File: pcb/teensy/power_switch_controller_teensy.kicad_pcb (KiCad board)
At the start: 2 copper layers, 77.5 x 40.6 mm, 23 parts, among them P1 PWR_JACK_2.5x5.5_SMD_RA, P2 HEADER_01X03_SMD_RA, P3 HEADER_01X03_SMD_RA, P4 HEADER_01X03_SMD_RA, P5 BNC_DOUBLE_RA, P6 HEADER_01X02_SMD_RA, P7 HEADER_01X02_SMD_RA, SW1 KT_SWITCH

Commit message: More progress towards v1.0.
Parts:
- removed C3, C4, C5: 10uF, power_switch_controller_teensy:SM1210
- removed D1, D2: diode_schottky_15V_1A, power_switch_controller_teensy:DO-214BA
- removed D3, D4: diode_schottky_45V_10A, power_switch_controller_teensy:CFP15
- removed MNT_HOLE1, MNT_HOLE2, MNT_HOLE3: MNT_HOLE, power_switch_controller_teensy:MNT_HOLE
- removed P2, P3, P4: HEADER_01X03_SMD_RA, power_switch_controller_teensy:Header_3_Pin_SMD_RA
- removed P5: BNC_DOUBLE_RA, power_switch_controller_teensy:BNC_DOUBLE
- removed P6, P7: HEADER_01X02_SMD_RA, power_switch_controller_teensy:Header_2_Pin_SMD_RA
- removed REG1: CONV_DC_DC_5V_1A, power_switch_controller_teensy:DC_DC_CONV_R78C
- removed TEENSY1: TEENSY_3_2, power_switch_controller_teensy:TEENSY_3
- added L1: LED_24V, power_switch_controller_teensy:LED_555-3XXX, F.Cu at (82.5, 99.7)
- added L2: LED_24V, power_switch_controller_teensy:LED_555-3XXX, F.Cu at (114.3, 109.2)
- added L3: LED_24V, power_switch_controller_teensy:LED_555-3XXX, F.Cu at (111.8, 109.2)
- added L4: LED_24V, power_switch_controller_teensy:LED_555-3XXX, F.Cu at (109.2, 109.2)
- added L5: LED_24V, power_switch_controller_teensy:LED_555-3XXX, F.Cu at (106.7, 109.2)
- added L6: LED_24V, power_switch_controller_teensy:LED_555-3XXX, F.Cu at (104.1, 109.2)
- added L7: LED_24V, power_switch_controller_teensy:LED_555-3XXX, F.Cu at (101.6, 109.2)
- added L8: LED_24V, power_switch_controller_teensy:LED_555-3XXX, F.Cu at (99.1, 109.2)
- added L9: LED_24V, power_switch_controller_teensy:LED_555-3XXX, F.Cu at (96.5, 109.2)
- added U1: TLE7230R, power_switch_controller_teensy:PG-DSO-36, B.Cu at (123.2, 99.7)
- C2: value 10uF -> 0.1uF
- MDT1: value MODULAR_DEVICE_TEENSY -> MODULAR_DEVICE_TEENSY_MALE
- P1: value PWR_JACK_2.5x5.5_SMD_RA -> HEADER_02X08_SMD; footprint power_switch_controller_teensy:DCJACK_2PIN_HIGHCURRENT_SMD_RA -> power_switch_controller_teensy:HEADER_02x08_SMD; moved to F.Cu
- SW1: value KT_SWITCH -> SPST_SLIDE_AS; footprint power_switch_controller_teensy:KT_SWITCH -> power_switch_controller_teensy:SPST_SLIDE_AS
- moved C2 60.3 mm to (123.2, 111.1), turned to 0 degrees
- moved P1 26.7 mm to (105.4, 99.7)
- moved SW1 21.6 mm to (86.4, 99.7), turned to 0 degrees
- moved C1 20.7 mm to (83.8, 91.4), turned to 180 degrees
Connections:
- C2 pad 1: +5V -> VEE
- MDT1 pad 10: /D10 -> /CS
- MDT1 pad 11: /D11 -> /MOSI
- MDT1 pad 12: /D12 -> /MISO
- MDT1 pad 13: /D13 -> /SCK
- MDT1 pad 14: /D14 -> (no net)
- MDT1 pad 15: /D15 -> (no net)
- MDT1 pad 16: /D16 -> (no net)
- MDT1 pad 17: /D17 -> (no net)
- MDT1 pad 18: /D18 -> (no net)
- MDT1 pad 19: /D19 -> (no net)
- MDT1 pad 2: /D2 -> /RESET
- MDT1 pad 20: /D20 -> (no net)
- MDT1 pad 21: /D21 -> (no net)
- MDT1 pad 22: /D22 -> (no net)
- MDT1 pad 23: /D23 -> (no net)
- MDT1 pad 24: /D24 -> (no net)
- MDT1 pad 25: /D25 -> (no net)
- MDT1 pad 28: /D28 -> (no net)
- MDT1 pad 29: /D29 -> (no net)
- MDT1 pad 3: /D3 -> /PWM
- MDT1 pad 30: /D30 -> (no net)
- MDT1 pad 3V3: /3V3 -> (no net)
- MDT1 pad 4: /D4 -> (no net)
- MDT1 pad 5: /D5 -> (no net)
- MDT1 pad 6: /D6 -> (no net)
- MDT1 pad 9: /D9 -> (no net)
- MDT1 pad AGND: /AGND -> (no net)
- MDT1 pad AREF: /AREF -> (no net)
- MDT1 pad DAC: /DAC -> (no net)
- P1 pad 1: VAA -> VDD
- P1 pad 2: GND -> /OUT0
- P1 pad 3: (no net) -> VDD
- SW1 pad 1: (no net) -> VDD
- SW1 pad 3: GND -> /LED_PWR
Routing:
- net (no net): track 0.00 -> 570.8 mm, vias 0 -> 4
- net /OUT3: track 0.00 -> 89.8 mm, vias 0 -> 2
- net VAA: track 85.8 -> 0.00 mm, vias 2 -> 0
- net /OUT4: track 0.00 -> 73.9 mm
- net /PROG: track 57.7 -> 0.00 mm
- net /RX1: track 56.4 -> 0.00 mm, vias 1 -> 0
- net /LED_PWR: track 0.00 -> 51.4 mm, vias 0 -> 1
- net /OUT6: track 0.00 -> 50.6 mm
- net /AREF: track 45.5 -> 0.00 mm, vias 1 -> 0
- net /TX3: track 45.5 -> 0.00 mm, vias 1 -> 0
- net /TX1: track 44.1 -> 0.00 mm, vias 1 -> 0
- net /RX3: track 40.9 -> 0.00 mm
- net /BNC_A: track 40.4 -> 0.00 mm
- net /BNC_B: track 34.7 -> 0.00 mm
- net /D24: track 32.2 -> 0.00 mm
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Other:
- board size 77.5 x 40.6 mm -> 63.5 x 40.6 mm
- board text added: "0"
- board text added: "1"
- board text added: "2"
- board text added: "3"
- board text added: "4"
- board text added: "5"
- board text added: "6"
- board text added: "7"
- board text added: "Janelia Modular Device power_switch_controller model_number: 1111 07/2016 ver 1.0 teensy"
- board text added: "Lights"
- board text added: "https://github.com/janelia-modular-devices"
- board text removed: "+9-42VDC"
- board text removed: "2.5x5.5 Center +"
- board text removed: "5V"
- board text removed: "Janelia Modular Device power_switch_controller_teensy 07/2016 ver 1.0"
- board text removed: "Serial1"
- board text removed: "Serial2"
- board text removed: "Serial3"

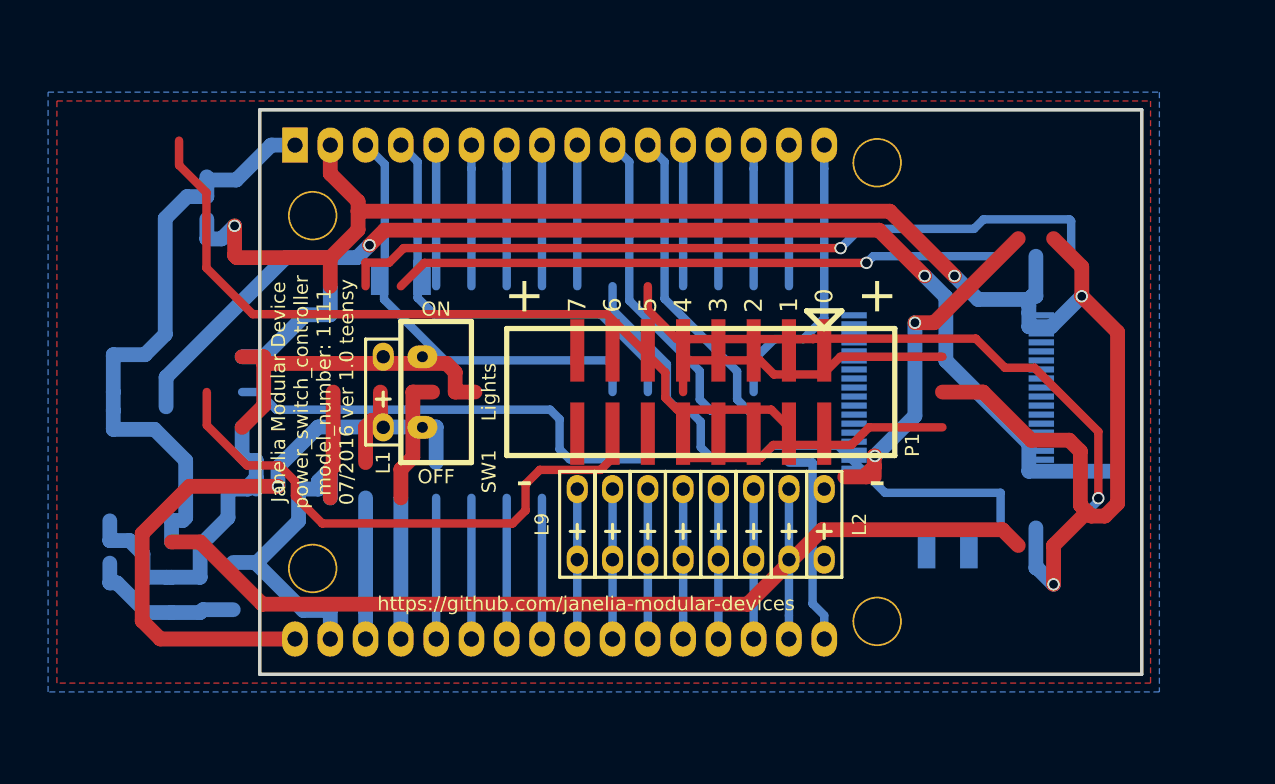
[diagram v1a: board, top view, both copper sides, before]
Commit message: Finished teensy pcb v1.0.
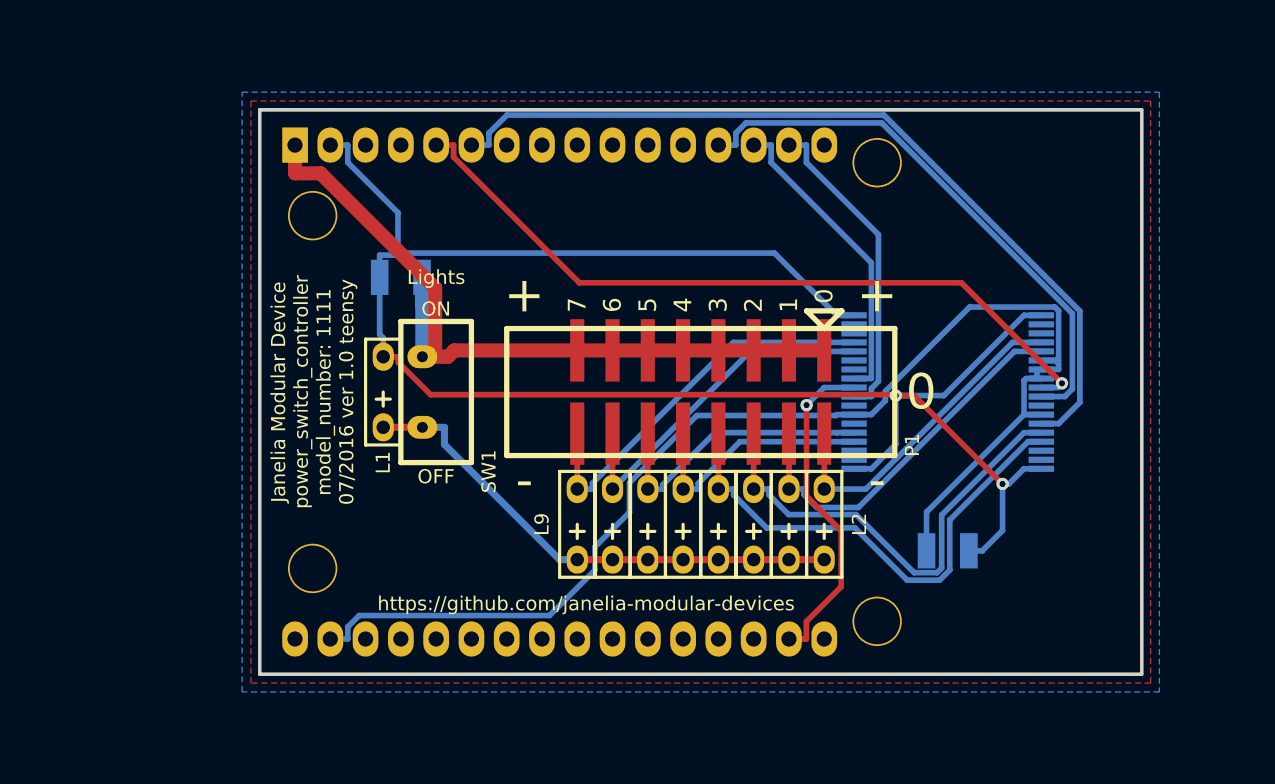
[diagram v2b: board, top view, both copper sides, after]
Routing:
- net (no net): track 570.8 -> 0.00 mm, vias 4 -> 0
- net VEE: track 22.3 -> 91.1 mm
- net /OUT4: track 73.9 -> 18.0 mm
- net VDD: track 110.8 -> 55.3 mm, vias 1 -> 0
- net /OUT3: track 89.8 -> 36.4 mm, vias 2 -> 0
- net /PWM: track 10.2 -> 61.0 mm
- net /RESET: track 10.2 -> 54.3 mm, vias 0 -> 1
- net GND: track 174.9 -> 132.4 mm, vias 4 -> 2
- net /CS: track 10.2 -> 40.2 mm
- net /OUT6: track 50.6 -> 25.5 mm
- net /OUT0: track 0.00 -> 24.0 mm
- net /SCK: track 1.70 -> 24.1 mm, vias 0 -> 1
- net /OUT7: track 10.2 -> 28.5 mm
- net /OUT1: track 10.3 -> 27.6 mm
- net /LED_PWR: track 51.4 -> 36.4 mm, vias 1 -> 0
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- added copper zone on F.Cu, net VDD
- removed copper zone on F.Cu, net GND
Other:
- net class Default: clearance 0.2 -> 0.0254; trace_width 0.25 -> 0.254; via_dia 0.6 -> 0.889; via_drill 0.4 -> 0.635
- net class GND added: clearance 0.1016, trace_width 0.4064, via_dia 0.889, via_drill 0.635
- net class LEDPOWER added: clearance 0.254, trace_width 0.508, via_dia 0.889, via_drill 0.635
- net class POWER added: clearance 0.254, trace_width 0.8128, via_dia 0.889, via_drill 0.635
- net class Power removed
- net class SIGNAL added: clearance 0.1016, trace_width 0.4064, via_dia 0.889, via_drill 0.635
- net class SUPERPOWER added: clearance 0.254, trace_width 1.016, via_dia 0.889, via_drill 0.635
- net class Signal removed
- rule trace_clearance: 0.2 -> 0.0254

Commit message: Finished pcb v1.1.
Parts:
- MDT1: footprint power_switch_controller_teensy:MODULAR_DEVICE_TEENSY -> power_switch_controller_teensy:MODULAR_DEVICE_TEENSY_MALE
- moved C2 6.54 mm to (128.9, 108.0)
- moved U1 6.54 mm to (128.9, 96.5)
- moved L7 4.49 mm to (104.8, 106.0)
- moved L2 4.49 mm to (117.5, 106.0)
- moved L3 4.49 mm to (114.9, 106.0)
- moved L4 4.49 mm to (112.4, 106.0)
- moved L5 4.49 mm to (109.9, 106.0)
- moved L6 4.49 mm to (107.3, 106.0)
- moved L8 4.49 mm to (102.2, 106.0)
- moved L9 4.49 mm to (99.7, 106.0)
- moved P1 4.49 mm to (108.6, 96.5)
- moved C1 1.91 mm to (85.7, 91.4)
- moved L1 1.91 mm to (84.5, 99.7)
- moved SW1 1.91 mm to (88.3, 99.7)
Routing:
- net VEE: track 91.1 -> 109.8 mm
- net /PWM: track 61.0 -> 54.2 mm, vias 0 -> 1
- net /OUT6: track 25.5 -> 31.3 mm, vias 0 -> 1
- net /MISO: track 23.0 -> 28.1 mm
- net /CS: track 40.2 -> 35.7 mm, vias 0 -> 1
- net /SCK: track 24.1 -> 28.5 mm
- net /RESET: track 54.3 -> 58.2 mm
- net GND: track 132.4 -> 136.2 mm, vias 2 -> 0
- net /OUT1: track 27.6 -> 30.2 mm, vias 0 -> 1
- net /OUT5: track 20.7 -> 23.2 mm
- net /OUT4: track 18.0 -> 20.5 mm
- net /OUT7: track 28.5 -> 31.0 mm, vias 0 -> 1
- net /MOSI: track 22.3 -> 20.5 mm
- net /OUT0: track 24.0 -> 25.3 mm, vias 0 -> 1
- net /OUT2: track 33.8 -> 35.0 mm
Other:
- board size 63.5 x 40.6 mm -> 69.8 x 40.6 mm
- board text added: "Janelia Modular Device power_switch_controller model_number: 1111 08/2016 ver 1.1 teensy"
- board text removed: "Janelia Modular Device power_switch_controller model_number: 1111 07/2016 ver 1.0 teensy"
